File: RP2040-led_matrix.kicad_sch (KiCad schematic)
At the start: 27 parts, among them J2 USB_C_Receptacle, SW2 SW_DIP_x01, U1 W25Q16JVSS, U2 RP2040, U4 NCP1117-1.5_SOT223, Y2 ABM8-272-T3

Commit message: improved design of the matrix
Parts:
- C13: renamed from C3; value 1u -> 10u
- C3: renamed from C4; value 1u -> 10u
- R5: renamed from R4; value 10k -> 100k
- renumbered C6 to C1, C15 to C10, C16 to C11, C18 to C12, C9 to C14, C10 to C15, C8 to C16, C7 to C2, C17 to C4, C11 to C6, C12 to C7, C13 to C8, C14 to C9, J2 to J1, R6 to R1, R7 to R2, R5 to R3, R1 to R4, SW2 to SW1, U2 to U1, U4 to U2, U1 to U3, Y2 to Y1

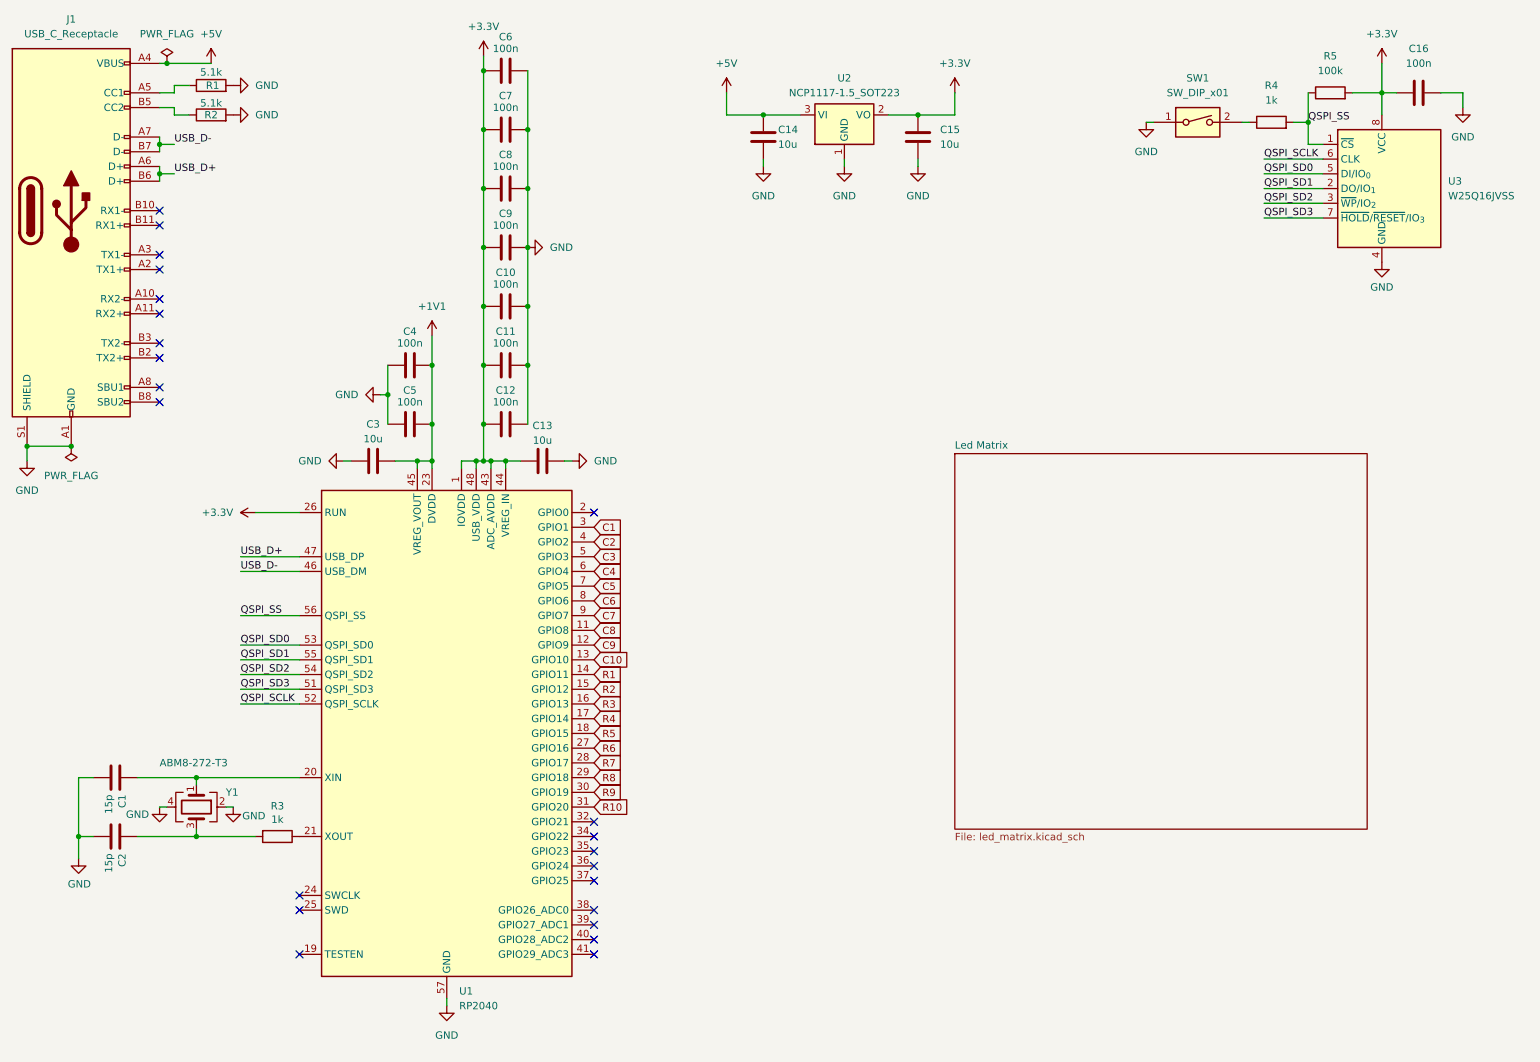
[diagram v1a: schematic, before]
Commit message: improved design and starting to layout the components
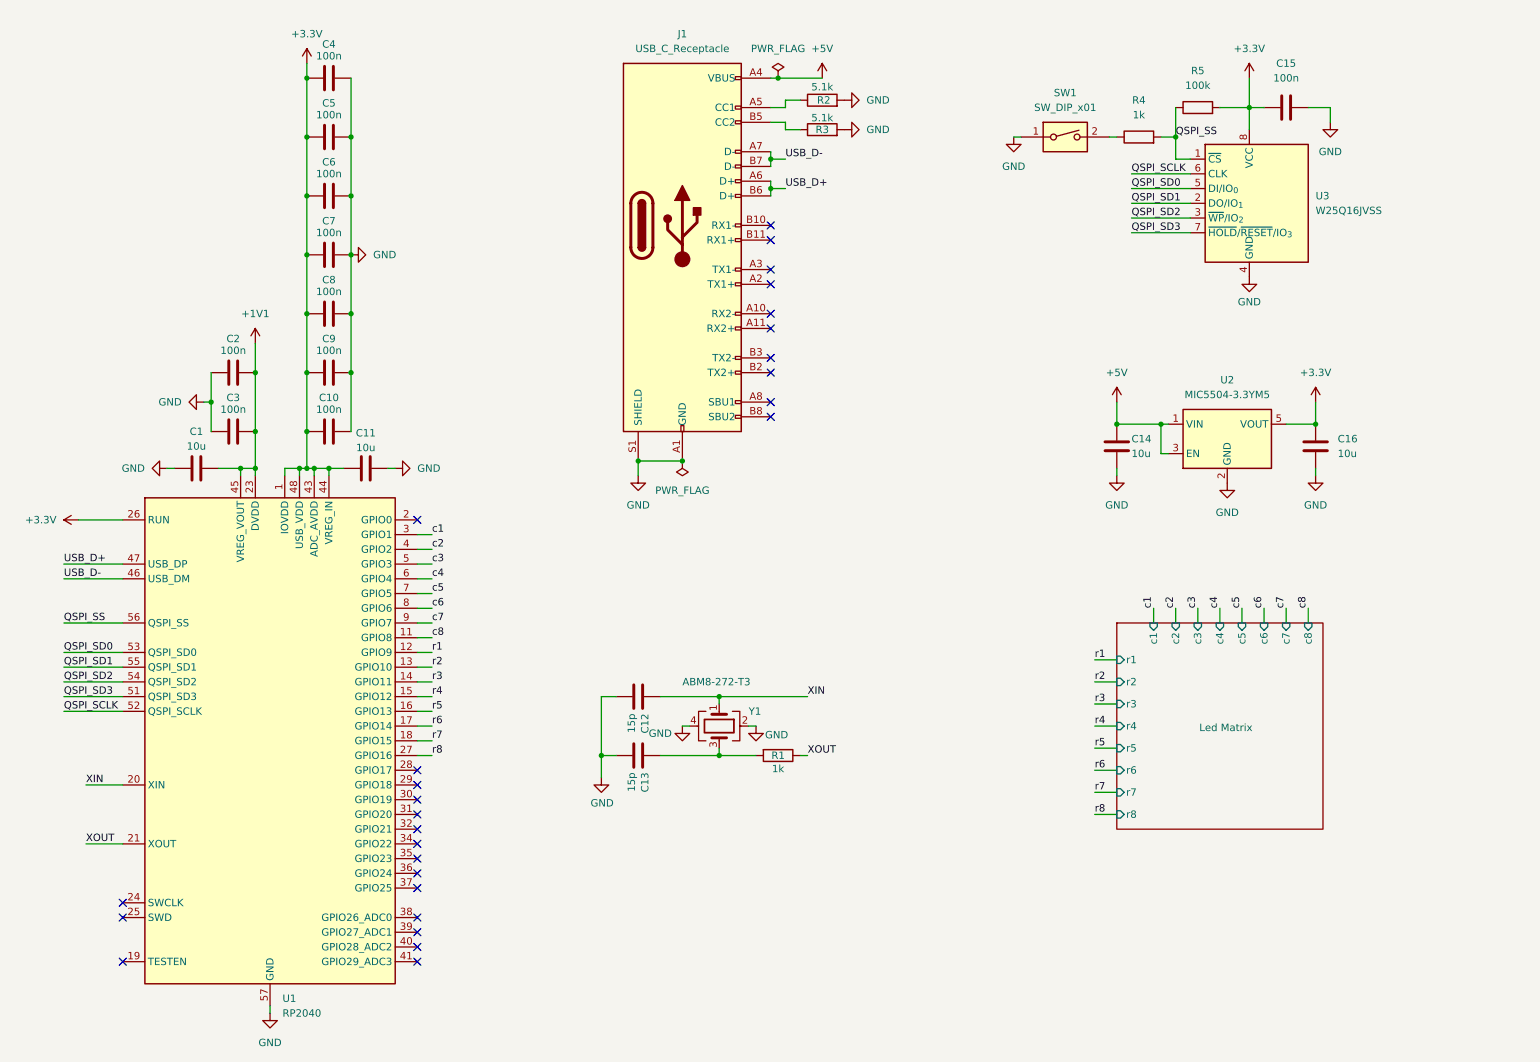
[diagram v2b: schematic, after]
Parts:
- removed U2: NCP1117-1.5_SOT223, Package_TO_SOT_SMD:SOT-223-3_TabPin2, symbol Regulator_Linear:NCP1117-1.5_SOT223
- added U2: MIC5504-3.3YM5, Package_TO_SOT_SMD:SOT-23-5, symbol Regulator_Linear:MIC5504-3.3YM5
- renumbered C3 to C1, C12 to C10, C13 to C11, C1 to C12, C2 to C13, C16 to C15, C15 to C16, C4 to C2, C5 to C3, C6 to C4, C7 to C5, C8 to C6, C9 to C7, C10 to C8, C11 to C9, R3 to R1, R1 to R2, R2 to R3
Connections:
- net +3.3V: now also U2.5 (VOUT)
- net +5V: now also U2.1 (VIN), U2.3 (EN)
- net GND: now also U2.2 (GND)
- net XIN: now reaches C12.1, U1.20 (XIN), Y1.1
- net XOUT: now reaches R1.1, U1.21 (XOUT)
- net C1 renamed c1
- net C10 renamed r2
- net C2 renamed c2
- net C3 renamed c3
- net C4 renamed c4
- net C5 renamed c5
- net C6 renamed c6
- net C7 renamed c7
- net C8 renamed c8
- net C9 renamed r1
- net R1 renamed r3
- net R10: no longer names the net of U1.31 (GPIO20)
- net R2 renamed r4
- net R3 renamed r5
- net R4 renamed r6
- net R5 renamed r7
- net R6 renamed r8
- net R7: no longer names the net of U1.28 (GPIO17)
- net R8: no longer names the net of U1.29 (GPIO18)
- net R9: no longer names the net of U1.30 (GPIO19)
- no-connect marks 23 -> 27
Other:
- sheet Led Matrix ports: added c1, c2, c3, c4, c5, c6, c7, c8, r1, r2, r3, r4, r5, r6, r7, r8; removed none
- moved on the sheet: C1, C10, C11, C12, C13, C14, C15, C16, C2, C3, C4, C5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
